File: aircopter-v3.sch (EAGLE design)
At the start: 44 parts, among them IC1 STF202-22T1G, M1 WIRELESS-NRF24L01, U2 GY-521MPU6050, Y1 20 MHz

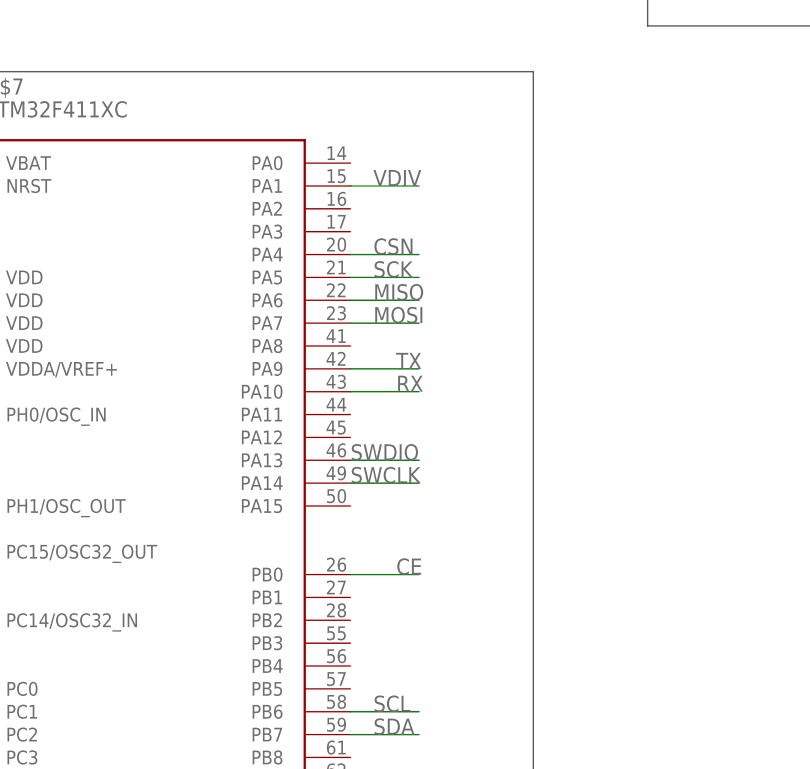
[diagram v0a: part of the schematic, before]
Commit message: redid motor section and planes, slightly moved mcu and radio, other small changes
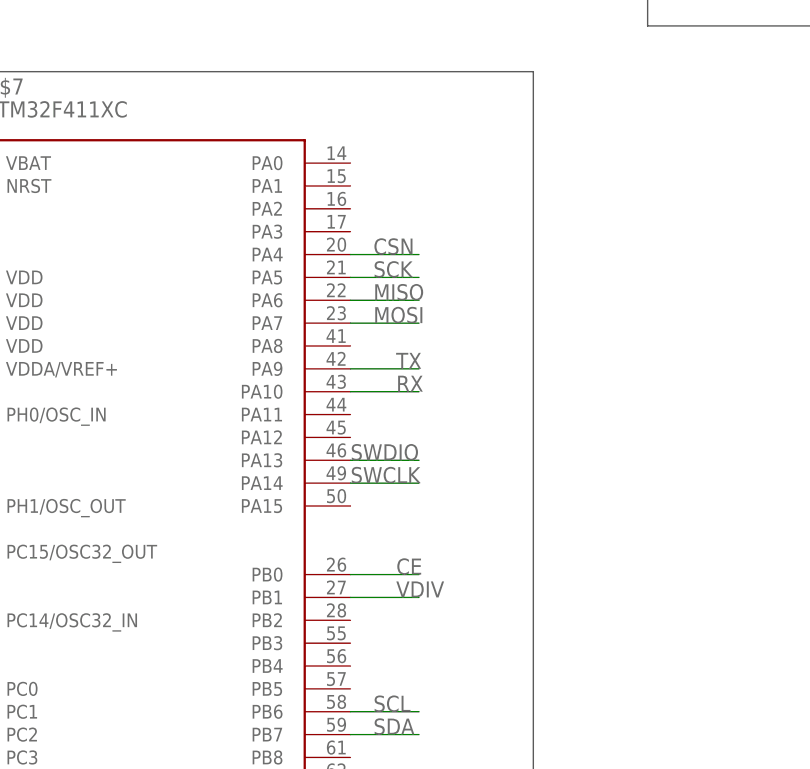
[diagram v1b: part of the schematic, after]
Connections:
- net VDIV: now also U$7.PB1; no longer U$7.PA1
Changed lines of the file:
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@@
 </segment>
 <segment>
-<pinref part="U$7" gate="G$1" pin="PA1"/>
-<wire x1="78.74" y1="-96.52" x2="86.36" y2="-96.52" width="0.1524" layer="91"/>
-<label x="81.28" y="-96.52" size="1.778" layer="95"/>
+<pinref part="U$7" gate="G$1" pin="PB1"/>
+<wire x1="78.74" y1="-142.24" x2="86.36" y2="-142.24" width="0.1524" layer="91"/>
+<label x="83.82" y="-142.24" size="1.778" layer="95"/>
 </segment>
 </net>
